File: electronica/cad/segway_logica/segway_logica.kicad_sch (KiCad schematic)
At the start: 11 parts, among them J20 Cable lógica-potencia 2x8, J4 Paro MPT0,5 1=GND 2=PARO (NC), J7 Encoder IZQ PT1,5 1=V 2=A 3=B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, J8 Encoder DER PT1,5 1=GND 2=A 3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

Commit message: electronica: expansión de la placa de lógica, tiras hembra junto a la ESP32-S3 (ELE-037)
Pedido del equipo: pines hembra en paralelo a la controladora para sumar
sensores (ultrasonido, infrarrojo).

- J24 y J25: tiras hembra 1x22 pegadas a cada hilera de A1, pin a pin.
  Huellas propias con el courtyard recortado del lado de A1.
- J26: tira hembra 1x6 de alimentación (GND, 3V3, 5V_MCU).
- J20.11 sin conexión también en la lógica; rótulos de cobre bajados
  para que el relleno GND no quede partido.
- generar_esquema.py: altura correcta de los conectores de una hilera
  (antes se pisaban las etiquetas y el comparador detectaba cortos).
- ERC 0, netlist coincidente, DRC 0 errores / 0 sin conectar / 0 paridad.
- SUP-72 y SUP-77 cambiados; SUP-78 y SUP-79 nuevos.

Co-Authored-By: Claude Opus 5.5 <noreply@anthropic.com>
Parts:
- added J24: Expansión ESP32 IZQ (A1.1-22), segway_modulos:Zocalo_expansion_izq_1x22_P2.54mm, symbol Connector_Generic:Conn_01x22
- added J25: Expansión ESP32 DER (A1.23-44), segway_modulos:Zocalo_expansion_der_1x22_P2.54mm, symbol Connector_Generic:Conn_01x22
- added J26: Alim. sensores 1-2 GND 3-4 3V3 5-6 5V, Connector_PinSocket_2.54mm:PinSocket_1x06_P2.54mm_Vertical, symbol Connector_Generic:Conn_01x06
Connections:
- net 3V3_MCU: now also J24.1 (Pin_1), J24.2 (Pin_2), J26.3 (Pin_3), J26.4 (Pin_4)
- net 5V_MCU: now also J24.21 (Pin_21), J26.5 (Pin_5), J26.6 (Pin_6)
- net ENC_DER_A: now also J24.7 (Pin_7)
- net ENC_DER_B: now also J24.8 (Pin_8)
- net ENC_IZQ_A: now also J24.4 (Pin_4)
- net ENC_IZQ_B: now also J24.5 (Pin_5)
- net GND: now also J24.22 (Pin_22), J25.1 (Pin_1), J25.21 (Pin_21), J25.22 (Pin_22), J26.1 (Pin_1), J26.2 (Pin_2); no longer J20.11 (Pin_11)
- net I2C_SCL: now also J24.9 (Pin_9)
- net I2C_SDA: now also J24.10 (Pin_10)
- net IMU_INT: now also J24.11 (Pin_11)
- net IN1_DER_MCU: now also J24.18 (Pin_18)
- net IN1_IZQ_MCU: now also J24.20 (Pin_20)
- net IN2_DER_MCU: now also J24.17 (Pin_17)
- net IN2_IZQ_MCU: now also J24.19 (Pin_19)
- net INA_ALERT: now also J24.12 (Pin_12)
- net PARO_CONT: now also J24.6 (Pin_6)
- net SERVO_DER_MCU: now also J24.16 (Pin_16)
- net SERVO_IZQ_MCU: now also J24.15 (Pin_15)
- net VBAT_ADC: now also J24.13 (Pin_13)
- net GPIO46: now reaches A1.14 (GPIO46)
- net GPIO46: now also J24.14 (Pin_14)
- net GPIO43: now reaches A1.24 (GPIO43/TX)
- net GPIO43: now also J25.2 (Pin_2)
- net GPIO44: now reaches A1.25 (GPIO44/RX)
- net GPIO44: now also J25.3 (Pin_3)
- net GPIO1: now reaches A1.26 (GPIO1)
- net GPIO1: now also J25.4 (Pin_4)
- net GPIO2: now reaches A1.27 (GPIO2)
- net GPIO2: now also J25.5 (Pin_5)
- net GPIO42: now reaches A1.28 (GPIO42)
- net GPIO42: now also J25.6 (Pin_6)
- net GPIO41: now reaches A1.29 (GPIO41)
- net GPIO41: now also J25.7 (Pin_7)
- net RST: now reaches A1.3 (RST)
- net RST: now also J24.3 (Pin_3)
- net GPIO40: now reaches A1.30 (GPIO40)
- net GPIO40: now also J25.8 (Pin_8)
- net GPIO39: now reaches A1.31 (GPIO39)
- net GPIO39: now also J25.9 (Pin_9)
- net GPIO38: now reaches A1.32 (GPIO38)
- net GPIO38: now also J25.10 (Pin_10)
- net GPIO37: now reaches A1.33 (GPIO37)
- net GPIO37: now also J25.11 (Pin_11)
- net GPIO36: now reaches A1.34 (GPIO36)
- net GPIO36: now also J25.12 (Pin_12)
- net GPIO35: now reaches A1.35 (GPIO35)
- net GPIO35: now also J25.13 (Pin_13)
- net GPIO0: now reaches A1.36 (GPIO0)
- net GPIO0: now also J25.14 (Pin_14)
- net GPIO45: now reaches A1.37 (GPIO45)
- net GPIO45: now also J25.15 (Pin_15)
- net GPIO48: now reaches A1.38 (GPIO48)
- net GPIO48: now also J25.16 (Pin_16)
- net GPIO47: now reaches A1.39 (GPIO47)
- net GPIO47: now also J25.17 (Pin_17)
- net GPIO21: now reaches A1.40 (GPIO21)
- net GPIO21: now also J25.18 (Pin_18)
- net GPIO20: now reaches A1.41 (GPIO20)
- net GPIO20: now also J25.19 (Pin_19)
- net GPIO19: now reaches A1.42 (GPIO19)
- net GPIO19: now also J25.20 (Pin_20)
- no-connect marks 24 -> 4

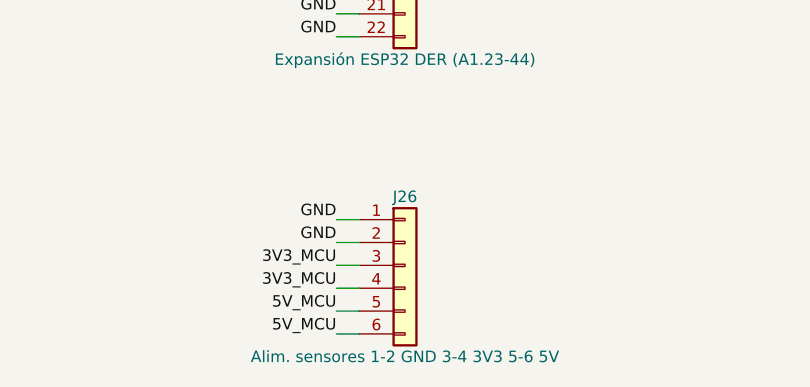
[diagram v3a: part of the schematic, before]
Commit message: electronica: rótulos de cobre, revisión independiente y control eléctrico (ELE-039)
- Rótulos de polaridad y de fusibles en el cobre de las dos placas,
  ubicados con ubicar_rotulos.py sin partir el relleno GND (SUP-14).
- Revisión independiente del conexionado contra las fichas: módulos,
  cable, polaridades y niveles correctos. Riesgos nuevos: A7 y A8 entran
  girados y queman (SUP-80), aleta de Q1 con tensión (SUP-20), I2C junto
  a PWM en el cable (SUP-81).
- auditoria_electrica.py: control repetible del sistema (cable, pines
  críticos, 5 V lejos de la ESP32, módulos girados, I2C, cuellos de
  pista, niveles). Informe: 0 fallas, 6 avisos.
- J26 reordenado con GND en el medio; textos de la Blue Pill en la
  especificación corregidos.
- ERC 0 y netlist coincidente; DRC 0/0/0 en las dos placas; salidas de
  fabricación regeneradas.

Co-Authored-By: Claude Opus 5.5 <noreply@anthropic.com>
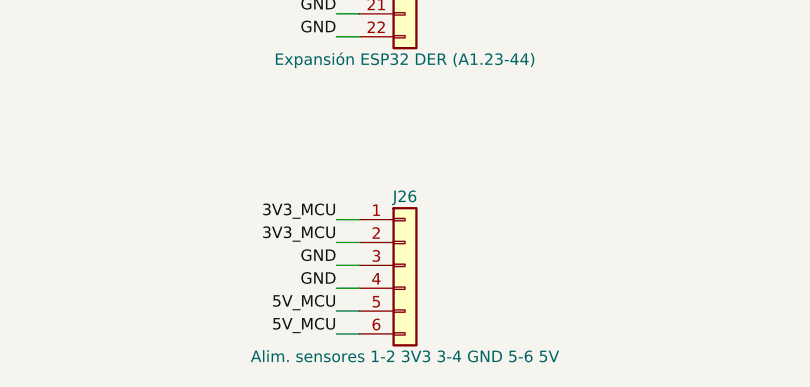
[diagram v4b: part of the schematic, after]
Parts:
- A2: Estado provisorio [H] (orden de pines [V]/[M]; zócalo estándar 1x08 (DEC-13); alimentado desde 3V3_PER; contorno del módulo pendiente de medida; codificación propuesta: retirar el pin 5 (XDA, sin uso) de la tira macho y tapar la posición 5 del zócalo, porque invertido llevaría 3V3_PER a INT y el VCC del módulo a PB14) | v0.4: huella segway_modulos:ROB-013_MPU6050_modulo_8p (1x08 + 2 NPTH de 3,2 mm, contorno supuesto); AD0 (pin 7) sin conexión: la pull-down del GY-521 fija 0x68 (SUP-36, SUP-66); sin pistas debajo -> provisorio [H] (orden de pines [V]/[M]; zócalo estándar 1x08 (DEC-13); alimentado desde 3V3_MCU; contorno del módulo pendiente de medida; codificación propuesta: retirar el pin 5 (XDA, sin uso) de la tira macho y tapar la posición 5 del zócalo, porque invertido llevaría 3V3_MCU a INT y el VCC del módulo a PB14) | v0.4: huella segway_modulos:ROB-013_MPU6050_modulo_8p (1x08 + 2 NPTH de 3,2 mm, contorno supuesto); AD0 (pin 7) sin conexión: la pull-down del GY-521 fija 0x68 (SUP-36, SUP-66); sin pistas debajo
- J26: value Alim. sensores 1-2 GND 3-4 3V3 5-6 5V -> Alim. sensores 1-2 3V3 3-4 GND 5-6 5V
- J4: Estado provisorio [H] (REQ-17; reemplaza al XH-3; sin contacto remoto hay que puentear 1-2; paso 2,54 mm distinto de J18 para no confundirlas) | v0.4: pasa a 2 polos al eliminar PARO_AUX y R26 (SUP-45, SUP-71); entrada directa a PB12 sin R25 ni C15 (SUP-58) -> provisorio [H] (REQ-17; reemplaza al XH-3; sin contacto remoto hay que puentear 1-2; paso 2,54 mm distinto de J18 para no confundirlas) | v0.4: pasa a 2 polos al eliminar PARO_AUX y R26 (SUP-45, SUP-71); entrada directa a GPIO6 sin R25 ni C15 (SUP-58)
- J7: Estado provisorio [H] (reemplaza al XH-4: los hilos del encoder se atornillan; A/B por color [H], invertirlos solo cambia el signo; calibre sin medir: puntera de 0,25 mm² si es AWG 26-28; alternativa MPT 0,5 de 2,54 mm con el mismo orden) | v0.4: pin 4 en 3V3_PER (V_ENC unido, R30 eliminada, SUP-53, SUP-64); C20 eliminado (SUP-69); pines 1 y 4 invertidos por ruteo (DEC-17) -> provisorio [H] (reemplaza al XH-4: los hilos del encoder se atornillan; A/B por color [H], invertirlos solo cambia el signo; calibre sin medir: puntera de 0,25 mm² si es AWG 26-28; alternativa MPT 0,5 de 2,54 mm con el mismo orden) | v0.4: pin 4 en 3V3_MCU (V_ENC unido, R30 eliminada, SUP-53, SUP-64); C20 eliminado (SUP-69); pines 1 y 4 invertidos por ruteo (DEC-17)
- J8: Estado provisorio [H] (reemplaza al XH-4: los hilos del encoder se atornillan; A/B por color [H], invertirlos solo cambia el signo; calibre sin medir: puntera de 0,25 mm² si es AWG 26-28; alternativa MPT 0,5 de 2,54 mm con el mismo orden) | v0.4: pin 4 en 3V3_PER (SUP-53); C21 eliminado (SUP-69) -> provisorio [H] (reemplaza al XH-4: los hilos del encoder se atornillan; A/B por color [H], invertirlos solo cambia el signo; calibre sin medir: puntera de 0,25 mm² si es AWG 26-28; alternativa MPT 0,5 de 2,54 mm con el mismo orden) | v0.4: pin 4 en 3V3_MCU (SUP-53); C21 eliminado (SUP-69)
- R13, R14, R15, R16: Estado provisorio [H] (montada; a 3V3_PER: sirve para colector abi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 -> provisorio [H] (montada; a 3V3_MCU: sirve para colector abi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; Fuente [ENERGIA] §6.5; [RM0008] §7.1.1 (Rev 6) (entrada flotante al reset); pull-up a 3V3_PER: con V_ENC = 5 V y salida de colector abierto, una pull-up a V_ENC con el divisor 1k/2k dejaba 5 · 2k/13k = 0,77 V en el pin, por debajo de VIH = 2,145 V ([DS-STM32] Tabla 36 p.61); huella THT de KiCad 10.0.7 (DEC-14, SUP-16) -> [ENERGIA] §6.5; [RM0008] §7.1.1 (Rev 6) (entrada flotante al reset); pull-up a 3V3_MCU: con V_ENC = 5 V y salida de colector abierto, una pull-up a V_ENC con el divisor 1k/2k dejaba 5 · 2k/13k = 0,77 V en el pin, por debajo de VIH = 2,145 V ([DS-STM32] Tabla 36 p.61); huella THT de KiCad 10.0.7 (DEC-14, SUP-16) | v0.6: las referencias al STM32 ([DS-STM32], [RM0008]) son de la v0.3; la controladora es la ESP32-S3 (DEC-16)
- R24: Estado provisorio [H] (pull-up desde 3V3_MCU: si cae 3V3_PER el pa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 -> provisorio [H] (pull-up desde 3V3_MCU: si cae 3V3_MCU el pa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
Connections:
- net 3V3_MCU: now also J26.1 (Pin_1), J26.2 (Pin_2); no longer J26.3 (Pin_3), J26.4 (Pin_4)
- net GND: now also J26.3 (Pin_3), J26.4 (Pin_4); no longer J26.1 (Pin_1), J26.2 (Pin_2)

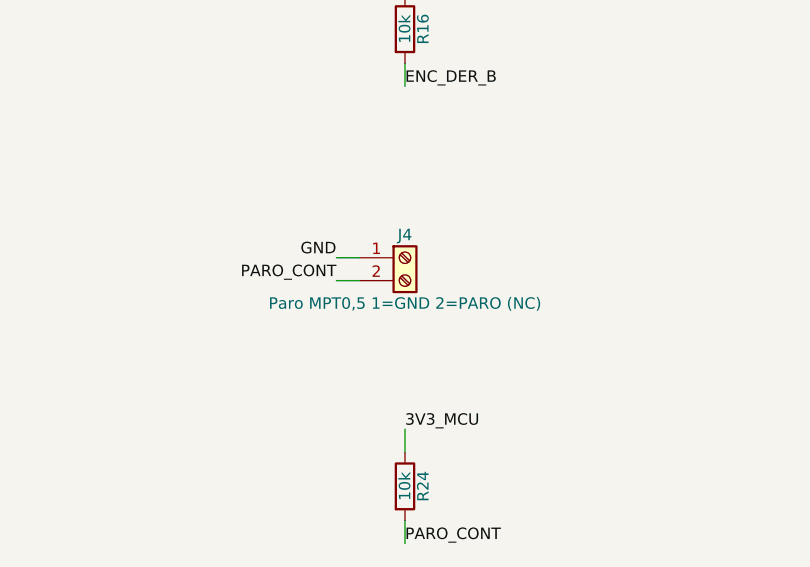
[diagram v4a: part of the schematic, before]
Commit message: electronica: PCB v0.2 de las dos placas, auditada (ELE-040)
- J3 y J4 pasan a pads para soldar el cable del interruptor y del paro.
- Montaje: A1-A4 en zócalo, A5-A8 soldados (DEC-20). A1 codificada:
  pin 24 cortado y posición tapada (revisión independiente: entraba
  girada o corrida y se quemaba).
- auditoria_electrica.py prueba giros y corrimientos de los módulos
  enchufados; 0 fallas, 3 avisos.
- Rótulos ambiguos de fusibles y VCC quitados; continuidad del cable
  J20 antes de enchufar; precinto en J3.
- Documentación v0.2, lista de compras, fabricación en rev-0.2.
- ERC 0, netlist coincidente, DRC 0/0/0 en las dos placas.

Co-Authored-By: Claude Opus 5.5 <noreply@anthropic.com>
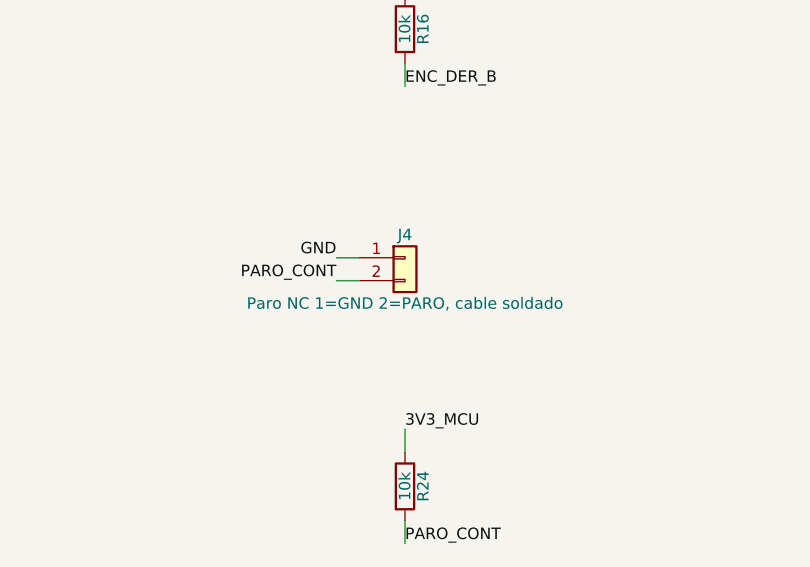
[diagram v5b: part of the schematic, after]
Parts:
- removed J4: Paro MPT0,5 1=GND 2=PARO (NC), TerminalBlock_Phoenix:TerminalBlock_Phoenix_MPT-0,5-2-2.54_1x02_P2.54mm_Horizontal, symbol Connector:Screw_Terminal_01x02
- added J4: Paro NC 1=GND 2=PARO, cable soldado, Connector_Wire:SolderWire-0.5sqmm_1x02_P4.6mm_D0.9mm_OD2.1mm, symbol Connector_Generic:Conn_01x02
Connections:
- net GND: now also J4.1 (Pin_1)
- net PARO_CONT: now also J4.2 (Pin_2)
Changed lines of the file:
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@@
 		(instances
 			(project "segway_logica"
-				(path "/1fe55f06-074c-4c3f-ac75-5515d0a43914"
+				(path "/af58779c-266d-433e-b714-b5cc63363289"
 					(reference "A1")
 					(unit 1)
@@
 		(instances
 			(project "segway_logica"
-				(path "/1fe55f06-074c-4c3f-ac75-5515d0a43914"
+				(path "/af58779c-266d-433e-b714-b5cc63363289"
 					(reference "A2")
 					(unit 1)
@@
 		(instances
 			(project "segway_logica"
-				(path "/1fe55f06-074c-4c3f-ac75-5515d0a43914"
+				(path "/af58779c-266d-433e-b714-b5cc63363289"
 					(reference "J7")
 					(unit 1)
@@
 		(instances
 			(project "segway_logica"
-				(path "/1fe55f06-074c-4c3f-ac75-5515d0a43914"
+				(path "/af58779c-266d-433e-b714-b5cc63363289"
 					(reference "J8")
 					(unit 1)
@@
 		(instances
 			(project "segway_logica"
-				(path "/1fe55f06-074c-4c3f-ac75-5515d0a43914"
+				(path "/af58779c-266d-433e-b714-b5cc63363289"
 					(reference "R13")
 					(unit 1)
@@
 		(instances
 			(project "segway_logica"
-				(path "/1fe55f06-074c-4c3f-ac75-5515d0a43914"
+				(path "/af58779c-266d-433e-b714-b5cc63363289"
 					(reference "R14")
 					(unit 1)
@@
 		(instances
 			(project "segway_logica"
-				(path "/1fe55f06-074c-4c3f-ac75-5515d0a43914"
+				(path "/af58779c-266d-433e-b714-b5cc63363289"
 					(reference "R15")
 					(unit 1)
@@
 		(instances
 			(project "segway_logica"
-				(path "/1fe55f06-074c-4c3f-ac75-5515d0a43914"
+				(path "/af58779c-266d-433e-b714-b5cc63363289"
 					(reference "R16")
 					(unit 1)
@@
 	)
 	(symbol
-		(lib_id "Connector:Screw_Terminal_01x02")
+		(lib_id "Connector_Generic:Conn_01x02")
 		(at 203.2 200.66 0)
 		(unit 1)
@@
 			)
 		)
-		(property "Value" "Paro MPT0,5 1=GND 2=PARO (NC)"
+		(property "Value" "Paro NC 1=GND 2=PARO, cable soldado"
 			(at 203.2 205.74 0)
 			(effects
@@
 			)
 		)
-		(property "Footprint" "TerminalBlock_Phoenix:TerminalBlock_Phoenix_MPT-0,5-2-2.54_1x02_P2.54mm_Horizontal"
+		(property "Footprint" "Connector_Wire:SolderWire-0.5sqmm_1x02_P4.6mm_D0.9mm_OD2.1mm"
 			(at 203.2 200.66 0)
 			(hide yes)
@@
 			)
 		)
-		(property "Description" "Generic screw terminal, single row, 01x02, script generated (kicad-library-utils/schlib/autogen/connector/)"
+		(property "Description" "Generic connector, single row, 01x02, script generated (kicad-library-utils/schlib/autogen/connector/)"
 			(at 203.2 200.66 0)
 			(hide yes)
@@
 			)
 		)
-		(property "Estado" "provisorio [H] (REQ-17; reemplaza al XH-3; sin contacto remoto hay que puentear 1-2; paso 2,54 mm distinto de J18 para no confundirlas) | v0.4: pasa a 2 polos al eliminar PARO_AUX y R26 (SUP-45, SUP-71); entrada directa a GPIO6 sin R25 ni C15 (SUP-58)"
+		(property "Estado" "v0.2 [M]: pads para soldar el cable del segundo contacto NC del hongo; sin ese contacto, puentear 1-2 (SUP-45)"
 			(at 203.2 200.66 0)
 			(hide yes)
@@
 		(instances
 			(project "segway_logica"
-				(path "/1fe55f06-074c-4c3f-ac75-5515d0a43914"
+				(path "/af58779c-266d-433e-b714-b5cc63363289"
 					(reference "J4")
 					(unit 1)
@@
 		(instances
 			(project "segway_logica"
-				(path "/1fe55f06-074c-4c3f-ac75-5515d0a43914"
+				(path "/af58779c-266d-433e-b714-b5cc63363289"
 					(reference "R24")
 					(unit 1)
@@
 		(instances
 			(project "segway_logica"
-				(path "/1fe55f06-074c-4c3f-ac75-5515d0a43914"
+				(path "/af58779c-266d-433e-b714-b5cc63363289"
 					(reference "J20")
 					(unit 1)
@@
 		(instances
 			(project "segway_logica"
-				(path "/1fe55f06-074c-4c3f-ac75-5515d0a43914"
+				(path "/af58779c-266d-433e-b714-b5cc63363289"
 					(reference "J24")
 					(unit 1)
@@
 		(instances
 			(project "segway_logica"
-				(path "/1fe55f06-074c-4c3f-ac75-5515d0a43914"
+				(path "/af58779c-266d-433e-b714-b5cc63363289"
 					(reference "J25")
 					(unit 1)
@@
 		(instances
 			(project "segway_logica"
-				(path "/1fe55f06-074c-4c3f-ac75-5515d0a43914"
+				(path "/af58779c-266d-433e-b714-b5cc63363289"
 					(reference "J26")
 					(unit 1)
@@
 		(instances
 			(project "segway_logica"
-				(path "/1fe55f06-074c-4c3f-ac75-5515d0a43914"
+				(path "/af58779c-266d-433e-b714-b5cc63363289"
 					(reference "#FLG01")
 					(unit 1)
@@
 		(instances
 			(project "segway_logica"
-				(path "/1fe55f06-074c-4c3f-ac75-5515d0a43914"
+				(path "/af58779c-266d-433e-b714-b5cc63363289"
 					(reference "#FLG02")
 					(unit 1)
@@
 		(instances
 			(project "segway_logica"
-				(path "/1fe55f06-074c-4c3f-ac75-5515d0a43914"
+				(path "/af58779c-266d-433e-b714-b5cc63363289"
 					(reference "#FLG03")
 					(unit 1)
